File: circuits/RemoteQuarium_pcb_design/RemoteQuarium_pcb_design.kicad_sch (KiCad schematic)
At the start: 51 parts, among them J1 Power_terminal, J10 LCD_pins, J11 Feeder_servo_pins, J12 ESP_pins, J13 PH_sensor_sockets, J14 Ph_sesnor-pins, J15 Power & D3-D4, J16 Reset_button_terminal, J2 ESP left side sockets, J3 ESP right side sockets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

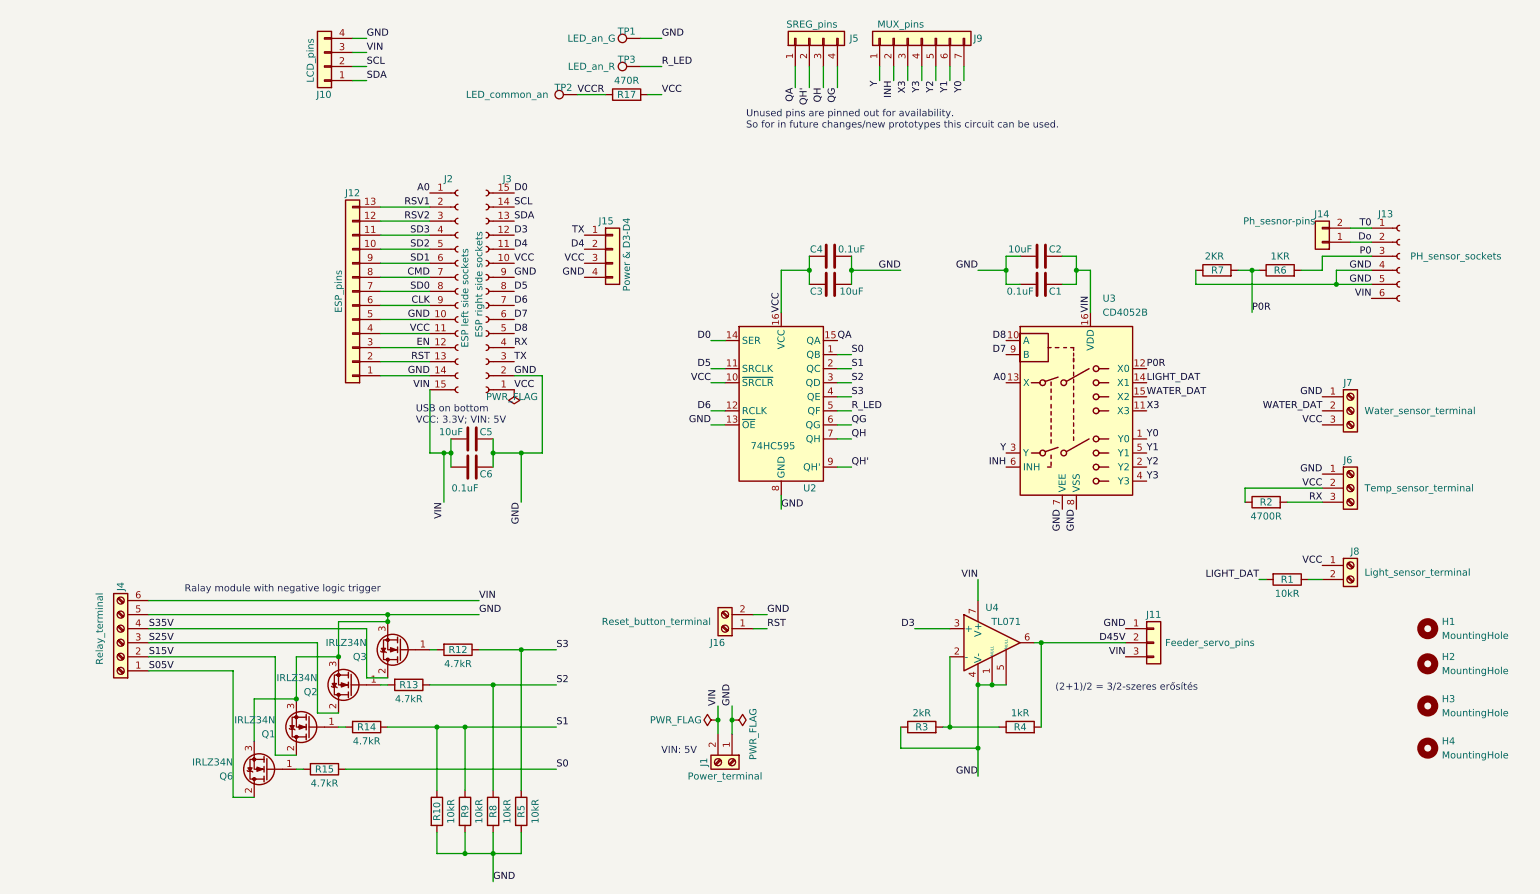
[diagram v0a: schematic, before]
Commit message: Working servo! Also added a few pages to thesis
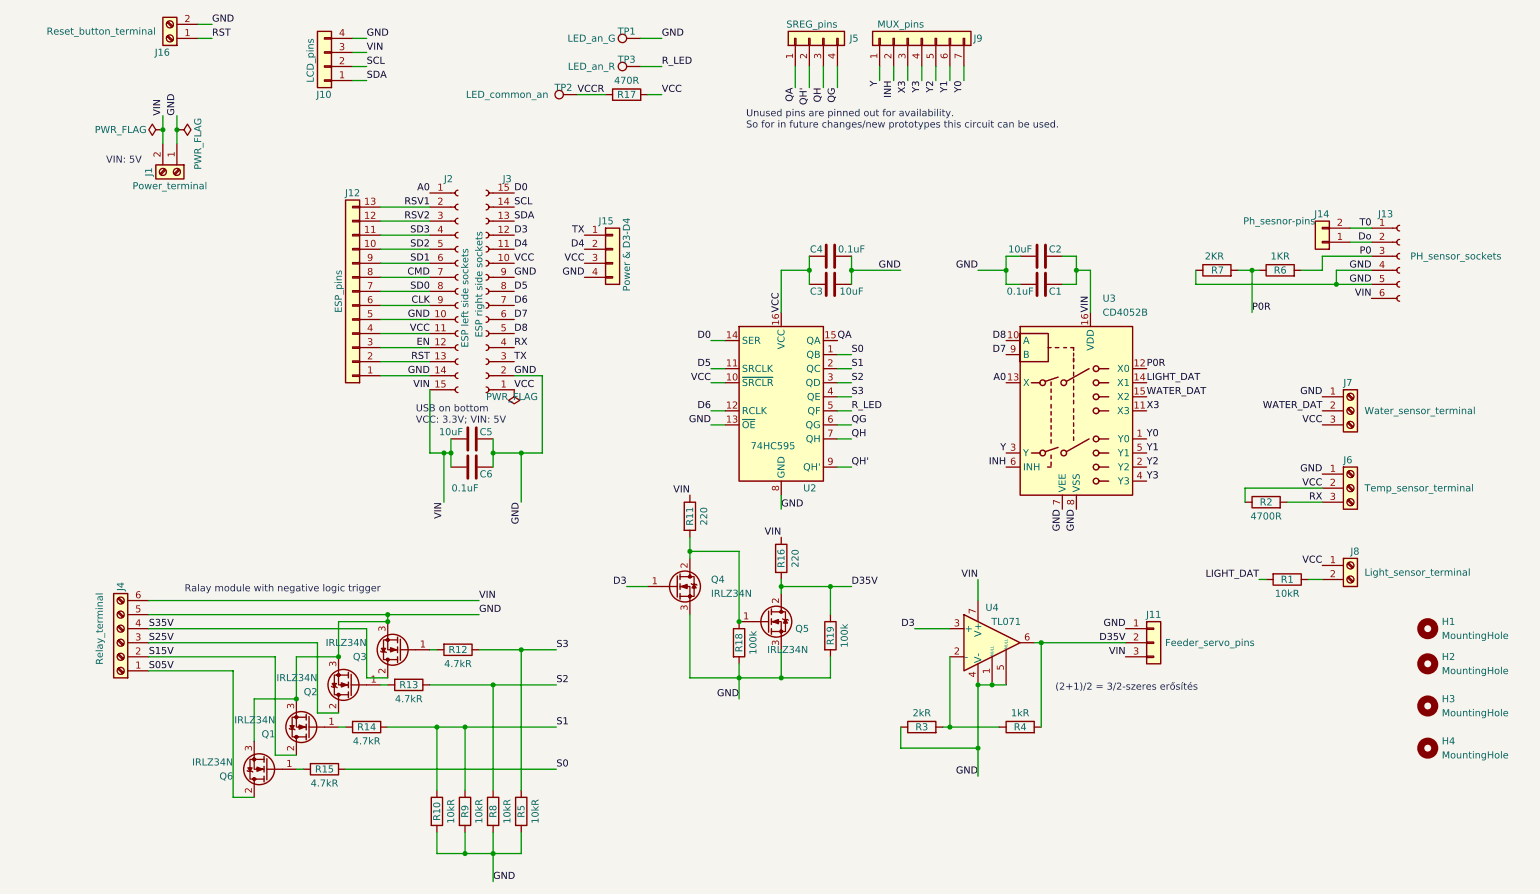
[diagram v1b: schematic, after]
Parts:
- added Q4, Q5: IRLZ34N, Package_TO_SOT_THT:TO-220-3_Vertical, symbol Transistor_FET:IRLZ34N
- added R11, R16: 220, Resistor_THT:R_Axial_DIN0207_L6.3mm_D2.5mm_P7.62mm_Horizontal, symbol Device:R
- added R18, R19: 100k, Resistor_THT:R_Axial_DIN0207_L6.3mm_D2.5mm_P7.62mm_Horizontal, symbol Device:R
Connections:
- net D3: now also Q4.1 (G)
- net GND: now also Q4.3 (S), Q5.3 (S), R18.2, R19.2
- net VIN: now also R11.1, R16.1
- net D45V renamed D35V
- net D35V: now also Q5.2 (D), R16.2, R19.1
- new net: Q4.2 (D), Q5.1 (G), R11.2, R18.1
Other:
- moved on the sheet: J1, J16

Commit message: Removed cleaning and waterchange from app since it won't be implemented and made the level shifter working
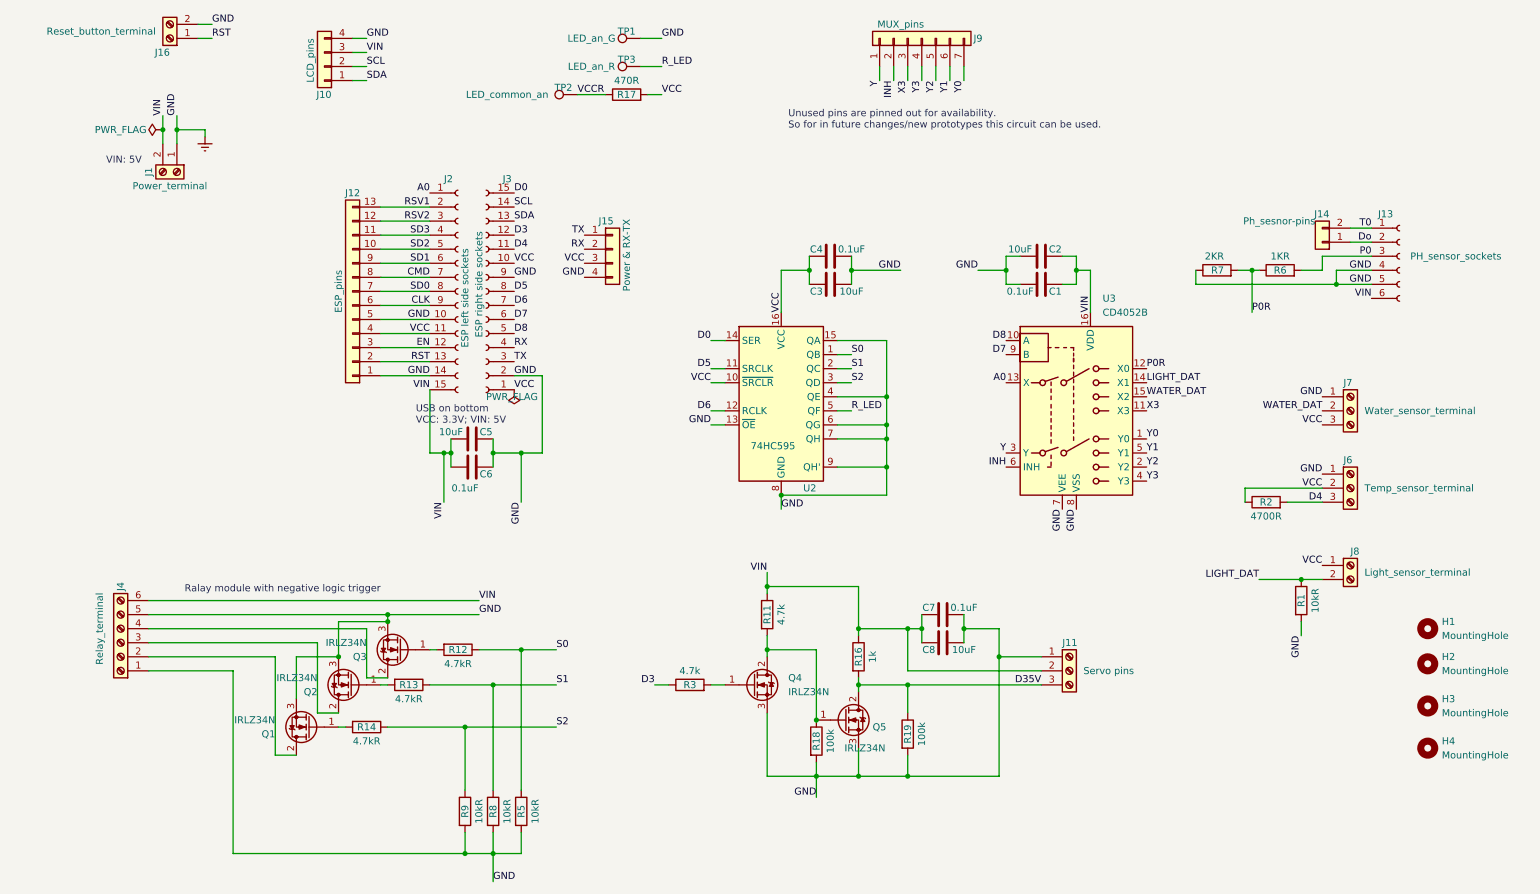
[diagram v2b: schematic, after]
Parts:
- removed J11: Feeder_servo_pins, Connector_PinHeader_2.54mm:PinHeader_1x03_P2.54mm_Vertical, symbol Connector_Generic:Conn_01x03
- removed J5: SREG_pins, Connector_PinHeader_2.54mm:PinHeader_1x04_P2.54mm_Vertical, symbol Connector_Generic:Conn_01x04
- removed Q6: IRLZ34N, Package_TO_SOT_THT:TO-220-3_Vertical, symbol Transistor_FET:IRLZ34N
- removed R10: 10kR, Resistor_THT:R_Axial_DIN0207_L6.3mm_D2.5mm_P7.62mm_Horizontal, symbol Device:R
- removed R15: 4.7kR, Resistor_THT:R_Axial_DIN0207_L6.3mm_D2.5mm_P7.62mm_Horizontal, symbol Device:R
- removed R4: 1kR, symbol Device:R
- removed U4: TL071, symbol Amplifier_Operational:TL071
- added C7: 0.1uF, Capacitor_THT:CP_Radial_D4.0mm_P1.50mm, symbol Device:C
- added C8: 10uF, Capacitor_THT:CP_Radial_D6.3mm_P2.50mm, symbol Device:C
- added J11: Servo pins, TerminalBlock_Phoenix:TerminalBlock_Phoenix_MPT-0,5-3-2.54_1x03_P2.54mm_Horizontal, symbol Connector:Screw_Terminal_01x03
- J15: value Power & D3-D4 -> Power & RX-TX
- R11: value 220 -> 4.7k
- R16: value 220 -> 1k
- R3: value 2kR -> 4.7k; footprint (none) -> Resistor_THT:R_Axial_DIN0207_L6.3mm_D2.5mm_P7.62mm_Horizontal
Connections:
- net QA is gone; now on net Earth: U2.15 (QA)
- net QG is gone; now on net Earth: U2.6 (QG)
- net QH is gone; now on net Earth: U2.7 (QH)
- net QH' is gone; now on net Earth: U2.9 (QH')
- net S05V is gone; now on net Earth: J4.1 (Pin_1)
- net D3: now also R3.1; no longer Q4.1 (G)
- net D35V: now also J11.3 (Pin_3)
- net D4: now also J6.3 (Pin_3), R2.2; no longer J15.2 (Pin_2)
- net LIGHT_DAT: now also J8.2 (Pin_2), R1.1; no longer R1.2
- net RX: now also J15.2 (Pin_2); no longer J6.3 (Pin_3), R2.2
- net S0: now also R12.1, R5.1
- net S1: now also R13.1, R8.1; no longer R14.1, R9.1
- net S2: now also R14.1, R9.1; no longer R13.1, R8.1
- net VIN: now also C7.2, C8.2, J11.2 (Pin_2)
- net at R3.2: now also Q4.1 (G)
- net GND renamed Earth
- net Earth: now also R1.2, U2.4 (QE), C7.1, C8.1, J11.1 (Pin_1); no longer R3.1
- net S15V: no longer names the net of J4.2 (Pin_2), Q1.2 (D)
- net S25V: no longer names the net of J4.3 (Pin_3), Q2.2 (D)
- removed net S3: R12.1, R5.1, U2.4 (QE)
- net S35V: no longer names the net of J4.4 (Pin_4), Q3.2 (D)
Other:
- note removed: "(2+1)/2 = 3/2-szeres erősítés"
- moved on the sheet: Q4, Q5, R1, R11, R16, R18, R19

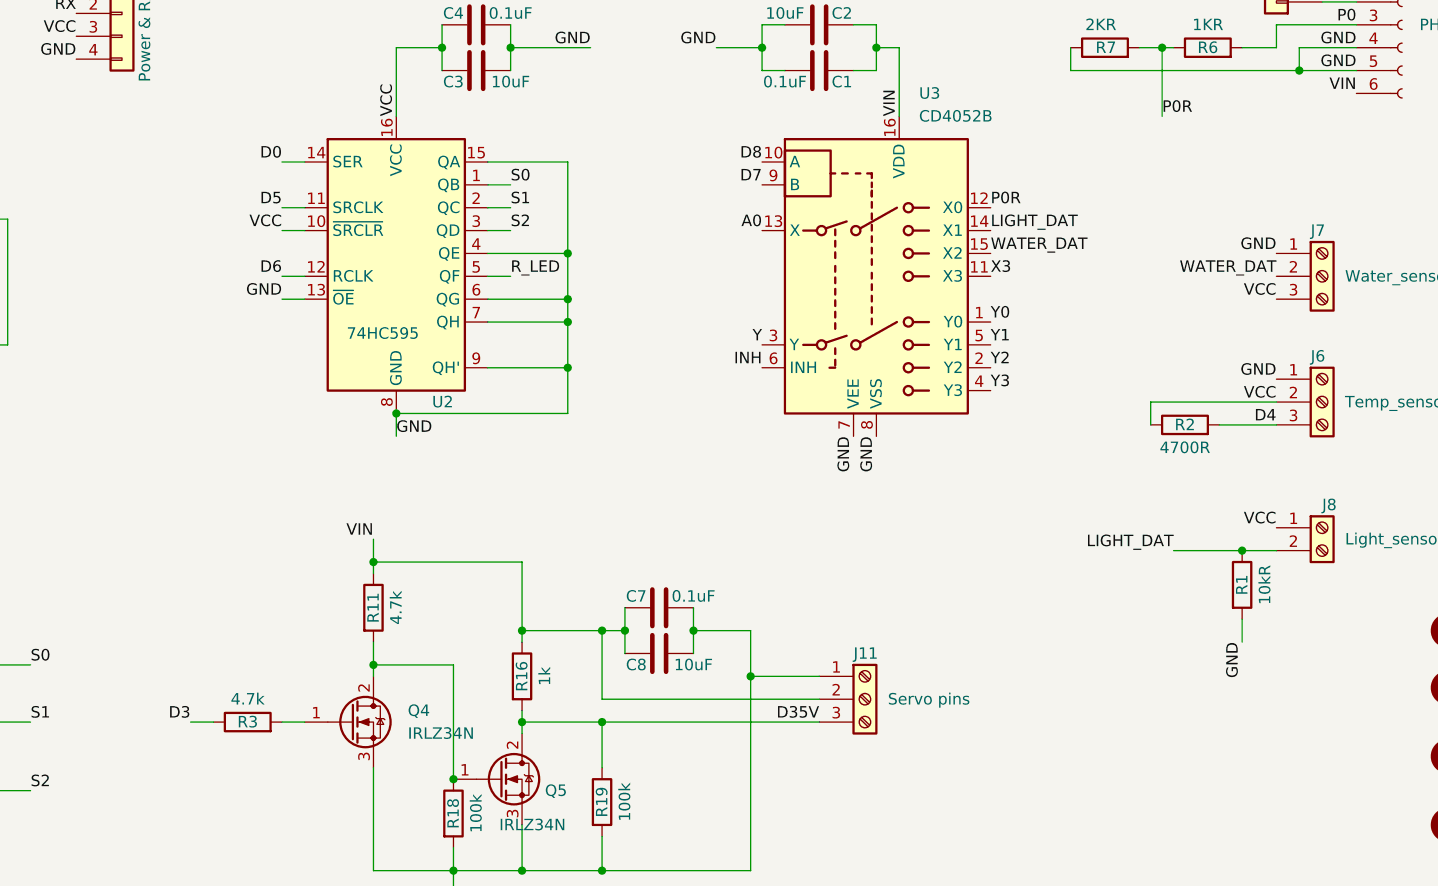
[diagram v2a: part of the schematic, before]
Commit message: Resolved ntp summer time change using timezones
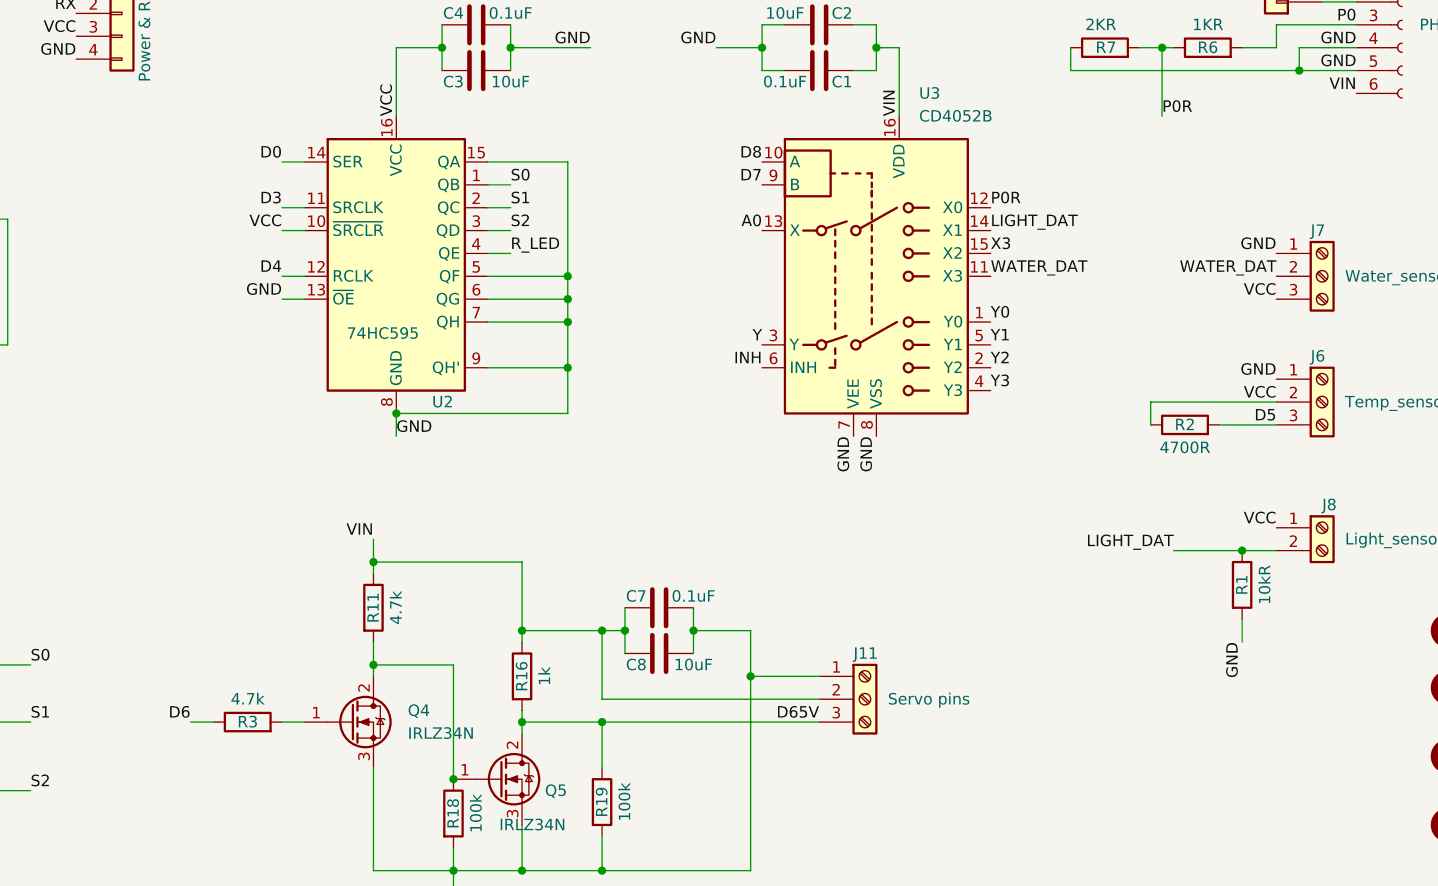
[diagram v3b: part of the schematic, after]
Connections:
- net D3: now also U2.11 (SRCLK); no longer R3.1
- net D4: now also U2.12 (RCLK); no longer J6.3 (Pin_3), R2.2
- net D5: now also J6.3 (Pin_3), R2.2; no longer U2.11 (SRCLK)
- net D6: now also R3.1; no longer U2.12 (RCLK)
- net Earth: now also U2.5 (QF); no longer U2.4 (QE)
- net R_LED: now also U2.4 (QE); no longer U2.5 (QF)
- net WATER_DAT: now also U3.11 (X3); no longer U3.15 (X2)
- net X3: now also U3.15 (X2); no longer U3.11 (X3)
- net D35V renamed D65V
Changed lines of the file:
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@@
   (junction (at 88.9 105.41) (diameter 0) (color 0 0 0 0)
   )
-  (junction (at 167.64 95.25) (diameter 0) (color 0 0 0 0)
-  )
   (junction (at 153.67 72.39) (diameter 0) (color 0 0 0 0)
   )
@@
   (junction (at 181.61 137.16) (diameter 0) (color 0 0 0 0)
   )
+  (junction (at 167.64 97.79) (diameter 0) (color 0 0 0 0)
+  )
   (junction (at 96.52 105.41) (diameter 0) (color 0 0 0 0)
   )
@@
     (stroke (width 0) (type default))
   )
+  (wire (pts (xy 161.29 95.25) (xy 158.75 95.25))
+    (stroke (width 0) (type default))
+  )
   (wire (pts (xy 101.6 140.97) (xy 101.6 166.37))
     (stroke (width 0) (type default))
@@
     (stroke (width 0) (type default))
   )
-  (wire (pts (xy 161.29 97.79) (xy 158.75 97.79))
+  (wire (pts (xy 158.75 97.79) (xy 167.64 97.79))
     (stroke (width 0) (type default))
   )
@@
     (stroke (width 0) (type default))
   )
-  (wire (pts (xy 167.64 95.25) (xy 167.64 100.33))
+  (wire (pts (xy 167.64 85.09) (xy 167.64 97.79))
     (stroke (width 0) (type default))
   )
@@
     (stroke (width 0) (type default))
   )
-  (wire (pts (xy 167.64 85.09) (xy 167.64 95.25))
-    (stroke (width 0) (type default))
-  )
   (wire (pts (xy 39.37 46.99) (xy 39.37 49.53))
     (stroke (width 0) (type default))
@@
     (stroke (width 0) (type default))
   )
+  (wire (pts (xy 167.64 97.79) (xy 167.64 100.33))
+    (stroke (width 0) (type default))
+  )
   (wire (pts (xy 96.52 173.99) (xy 96.52 177.8))
     (stroke (width 0) (type default))
   )
   (wire (pts (xy 88.9 102.87) (xy 88.9 105.41))
-    (stroke (width 0) (type default))
-  )
-  (wire (pts (xy 158.75 95.25) (xy 167.64 95.25))
     (stroke (width 0) (type default))
   )
@@
     (effects (font (size 1.27 1.27)) (justify left bottom))
   )
-  (label "D3" (at 125.73 147.32 180) (fields_autoplaced)
+  (label "D6" (at 125.73 147.32 180) (fields_autoplaced)
     (effects (font (size 1.27 1.27)) (justify right bottom))
   )
@@
     (effects (font (size 1.27 1.27)) (justify left bottom))
   )
-  (label "R_LED" (at 161.29 97.79 0) (fields_autoplaced)
+  (label "R_LED" (at 161.29 95.25 0) (fields_autoplaced)
     (effects (font (size 1.27 1.27)) (justify left bottom))
   )
@@
     (effects (font (size 1.27 1.27)) (justify right bottom))
   )
+  (label "X3" (at 214.63 95.25 0) (fields_autoplaced)
+    (effects (font (size 1.27 1.27)) (justify left bottom))
+  )
   (label "A0" (at 189.23 92.71 180) (fields_autoplaced)
     (effects (font (size 1.27 1.27)) (justify right bottom))
@@
     (effects (font (size 1.27 1.27)) (justify left bottom))
   )
-  (label "D4" (at 246.38 114.3 180) (fields_autoplaced)
+  (label "D5" (at 246.38 114.3 180) (fields_autoplaced)
     (effects (font (size 1.27 1.27)) (justify right bottom))
   )
@@
     (effects (font (size 1.27 1.27)) (justify left bottom))
   )
-  (label "X3" (at 214.63 97.79 0) (fields_autoplaced)
-    (effects (font (size 1.27 1.27)) (justify left bottom))
-  )
   (label "GND" (at 154.94 167.64 180) (fields_autoplaced)
     (effects (font (size 1.27 1.27)) (justify right bottom))
@@
     (effects (font (size 1.27 1.27)) (justify left bottom))
   )
+  (label "WATER_DAT" (at 214.63 97.79 0) (fields_autoplaced)
+    (effects (font (size 1.27 1.27)) (justify left bottom))
+  )
   (label "RX" (at 100.33 86.36 0) (fields_autoplaced)
     (effects (font (size 1.27 1.27)) (justify left bottom))
@@
     (effects (font (size 1.27 1.27)) (justify left bottom))
   )
-  (label "D6" (at 135.89 97.79 180) (fields_autoplaced)
+  (label "D4" (at 135.89 97.79 180) (fields_autoplaced)
     (effects (font (size 1.27 1.27)) (justify right bottom))
   )
@@
     (effects (font (size 1.27 1.27)) (justify right bottom))
   )
-  (label "D5" (at 135.89 90.17 180) (fields_autoplaced)
+  (label "D3" (at 135.89 90.17 180) (fields_autoplaced)
     (effects (font (size 1.27 1.27)) (justify right bottom))
   )
@@
     (effects (font (size 1.27 1.27)) (justify left bottom))
   )
-  (label "D35V" (at 195.58 147.32 180) (fields_autoplaced)
+  (label "D65V" (at 195.58 147.32 180) (fields_autoplaced)
     (effects (font (size 1.27 1.27)) (justify right bottom))
   )
@@
     (effects (font (size 1.27 1.27)) (justify left bottom))
   )
-  (label "WATER_DAT" (at 214.63 95.25 0) (fields_autoplaced)
-    (effects (font (size 1.27 1.27)) (justify left bottom))
-  )
